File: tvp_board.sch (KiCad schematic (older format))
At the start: 57 parts, among them U1 TVP7002PZP, U4 SN74LVC2G17, U5 AP7361C, U6 TLV70033, U7 NCP703SN19T1G, U9 TLV70019, Y1 ACHL-27MHZ-EK

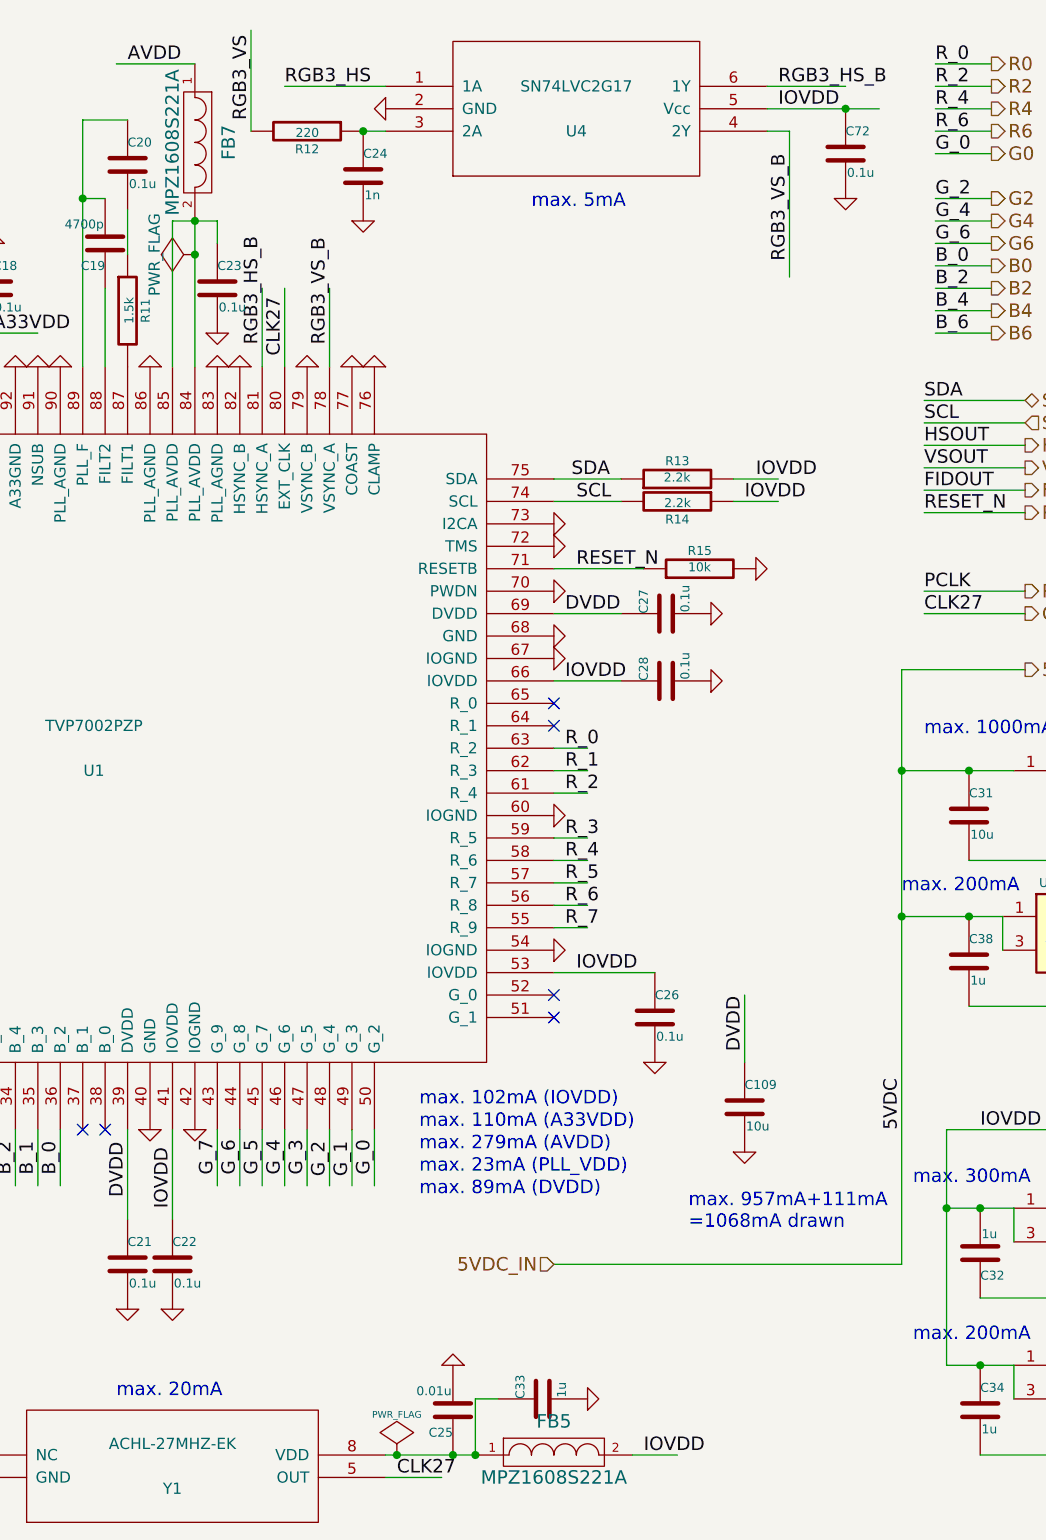
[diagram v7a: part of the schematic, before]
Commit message: add adc
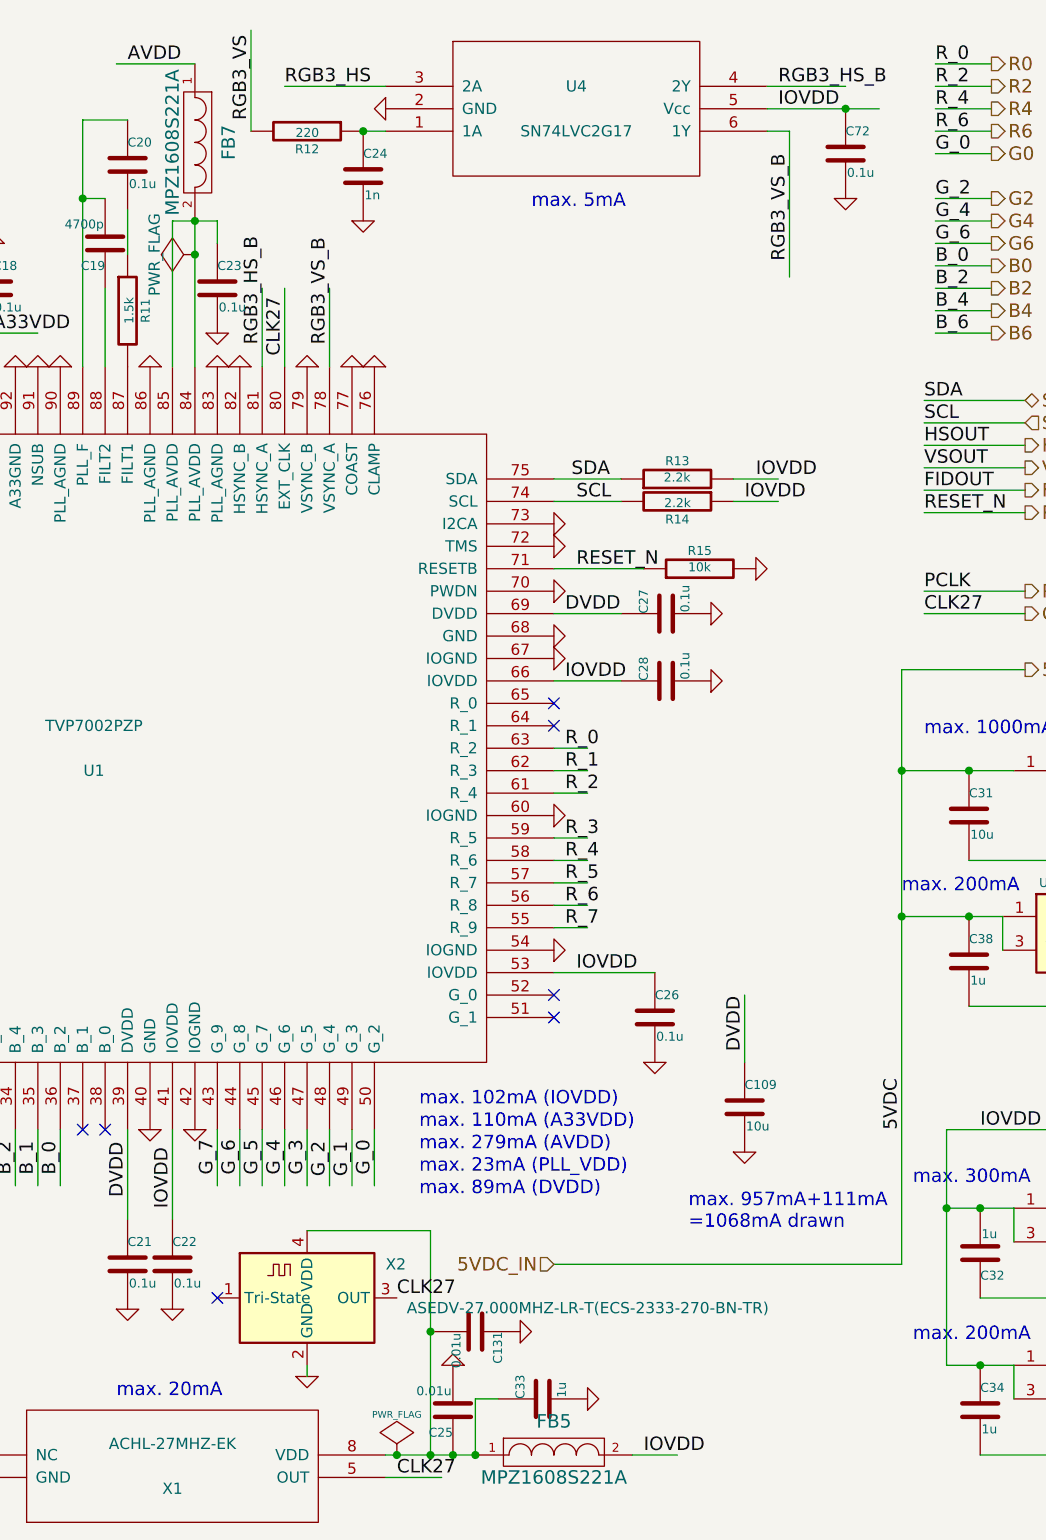
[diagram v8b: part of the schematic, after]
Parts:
- added C131: 0.01u, Capacitor_SMD:C_0603_1608Metric_Pad1.05x0.95mm_HandSolder, symbol ossc_board-rescue:C-RESCUE-ossc_board
- added X2: ASEDV-27.000MHZ-LR-T(ECS-2333-270-BN-TR), Oscillator:Oscillator_SMD_SeikoEpson_SG8002CE-4Pin_3.2x2.5mm_HandSoldering, symbol Oscillator:ECS-2520MV-xxx-xx
- renumbered Y1 to X1
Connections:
- wire segments 194 -> 199
- no-connect marks 8 -> 9
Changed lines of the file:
@@
 P 6100 7000
 AR Path="/53FD28BE" Ref="Y?"  Part="1"
-AR Path="/54FDD796/53FD28BE" Ref="Y1"  Part="1"
-F 0 "Y1" H 6100 6900 50  0000 C CNN
+AR Path="/54FDD796/53FD28BE" Ref="X1"  Part="1"
+F 0 "X1" H 6100 6900 50  0000 C CNN
 F 1 "ACHL-27MHZ-EK" H 6100 7100 50  0000 C CNN
 F 2 "custom_components:ACHL-OSC" H 6100 7000 50  0001 C CNN
@@
 Text Label 9450 3200 0    60   ~ 0
 CLK27
-$Comp
-L ossc_board-rescue:SN74LVC2G17 U4
-U 1 1 55BADF88
-P 7900 950
-F 0 "U4" H 7900 850 50  0000 C CNN
-F 1 "SN74LVC2G17" H 7900 1050 50  0000 C CNN
-F 2 "custom_components:SOT-23-6_Handsoldering" H 7900 950 50  0001 C CNN
-F 3 "DOCUMENTATION" H 7900 700 50  0001 C CNN
-	1    7900 950
-	1    0    0    -1
-$EndComp
 Text Label 9350 5500 1    60   ~ 0
 5VDC
@@
 	7350 6950 7450 6950
 Wire Wire Line
-	7100 6950 7350 6950
+	7100 6950 7250 6950
 Wire Wire Line
 	9550 5850 9550 6550
@@
 	0    -1   -1   0
 $EndComp
+$Comp
+L Oscillator:ECS-2520MV-xxx-xx X2
+U 1 1 5FDD2D83
+P 6700 6250
+F 0 "X2" H 7050 6400 50  0000 L CNN
+F 1 "ASEDV-27.000MHZ-LR-T(ECS-2333-270-BN-TR)" H 7144 6205 50  0000 L CNN
+F 2 "Oscillator:Oscillator_SMD_SeikoEpson_SG8002CE-4Pin_3.2x2.5mm_HandSoldering" H 7150 5900 50  0001 C CNN
+F 3 "https://www.ecsxtal.com/store/pdf/ECS-2520MV.pdf" H 6525 6375 50  0001 C CNN
+	1    6700 6250
+	1    0    0    -1
+$EndComp
+$Comp
+L ossc_board-rescue:GND-RESCUE-ossc_board #PWR0156
+U 1 1 5FDDB896
+P 6700 6600
+F 0 "#PWR0156" H 6700 6600 30  0001 C CNN
+F 1 "GND" H 6700 6530 30  0001 C CNN
+F 2 "" H 6700 6600 60  0001 C CNN
+F 3 "" H 6700 6600 60  0000 C CNN
+	1    6700 6600
+	1    0    0    -1
+$EndComp
+Wire Wire Line
+	6700 6550 6700 6600
+Wire Wire Line
+	6700 5950 7250 5950
+Wire Wire Line
+	7250 5950 7250 6400
+Connection ~ 7250 6950
+Wire Wire Line
+	7250 6950 7350 6950
+Text Label 7100 6250 0    60   ~ 0
+CLK27
+NoConn ~ 6300 6250
+$Comp
+L ossc_board-rescue:C-RESCUE-ossc_board C131
+U 1 1 5FE09243
+P 7450 6400
+F 0 "C131" H 7450 6500 40  0000 L CNN
+F 1 "0.01u" H 7456 6315 40  0000 L CNN
+F 2 "Capacitor_SMD:C_0603_1608Metric_Pad1.05x0.95mm_HandSolder" H 7488 6250 30  0001 C CNN
+F 3 "~" H 7450 6400 60  0000 C CNN
+	1    7450 6400
+	0    1    1    0
+$EndComp
+Connection ~ 7250 6400
+Wire Wire Line
+	7250 6400 7250 6950
+$Comp
+L ossc_board-rescue:GND-RESCUE-ossc_board #PWR081
+U 1 1 5FE0A5FF
+P 7650 6400
+F 0 "#PWR081" H 7650 6400 30  0001 C CNN
+F 1 "GND" H 7650 6330 30  0001 C CNN
+F 2 "" H 7650 6400 60  0001 C CNN
+F 3 "" H 7650 6400 60  0000 C CNN
+	1    7650 6400
+	0    -1   -1   0
+$EndComp
+$Comp
+L ossc_board-rescue:SN74LVC2G17 U4
+U 1 1 55BADF88
+P 7900 950
+F 0 "U4" H 7900 850 50  0000 C CNN
+F 1 "SN74LVC2G17" H 7900 1050 50  0000 C CNN
+F 2 "custom_components:SOT-23-6_Handsoldering" H 7900 950 50  0001 C CNN
+F 3 "DOCUMENTATION" H 7900 700 50  0001 C CNN
+	1    7900 950
+	1    0    0    1
+$EndComp
 $EndSCHEMATC
